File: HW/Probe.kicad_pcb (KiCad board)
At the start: 2 copper layers, 250 x 33 mm, 33 parts

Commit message: Update footprints for cam and distance sensor
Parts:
- CAM: footprint Connector_PinHeader_1.27mm:PinHeader_1x08_P1.27mm_Vertical -> Connector_PinHeader_2.54mm:PinHeader_1x08_P2.54mm_Vertical
- DIST: footprint Connector_PinHeader_1.27mm:PinHeader_1x05_P1.27mm_Vertical -> Connector_PinSocket_2.54mm:PinSocket_1x05_P2.54mm_Vertical
- moved CAM 4.44 mm to (231.3, 85.6)
- moved DIST 3.20 mm to (266.6, 99.5)
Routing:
- net SCL: track 242.5 -> 234.7 mm, vias 0 -> 2
- net DIST_INT: track 223.2 -> 227.8 mm
- net 3V3: track 225.2 -> 228.3 mm
- net CS: track 193.7 -> 196.3 mm
- net MOSI: track 182.7 -> 180.4 mm
- net MISO: track 187.4 -> 185.6 mm
- net +5V: track 264.8 -> 263.5 mm
- net SDA: track 237.1 -> 236.3 mm
- added copper zone on F.Cu, net GND

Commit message: Update PCB
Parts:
- removed NUCLEO-L432KC: NUCLEO-L432KC, Downloads:MODULE_NUCLEO-L432KC
- removed R: R, Resistor_SMD:R_0603_1608Metric
- removed USB: USB_C_Receptacle_USB2.0, KiCad:2171820001
- added Nucleo-L432KC1: ~, Library:MODULE_NUCLEO-L432KC, F.Cu at (67.5, 94.2)
- added R1: 100, Resistor_SMD:R_0603_1608Metric, F.Cu at (57.2, 81.1)
- added R2: 5.1K, Resistor_SMD:R_0603_1608Metric, F.Cu at (34.7, 93.0)
- added R3: 5.1K, Resistor_SMD:R_0603_1608Metric, F.Cu at (34.7, 96.1)
- added USB1: USB4110-GF-A_REVB, Library:GCT_USB4110-GF-A_REVB, F.Cu at (28.7, 94.5)
- CAM1: renamed from CAM; footprint Connector_PinHeader_2.54mm:PinHeader_1x08_P2.54mm_Vertical -> Connector_PinSocket_2.54mm:PinSocket_1x08_P2.54mm_Vertical
- H1, H10, H11, H12, H13, H14, H17, H18, H19, H2, H20, H3, H4, H5, H6, H7, H8, H9: footprint MountingHole:MountingHole_3.2mm_M3_Pad -> MountingHole:MountingHole_3.2mm_M3_Pad_Via
- moved LSR_PWR1 3.48 mm to (96.5, 92.8), turned to 180 degrees
- moved DIST1 1.30 mm to (265.3, 99.5)
- moved LED_SIG1 0.73 mm to (96.5, 104.2)
- moved LSR_SIG1 0.73 mm to (96.5, 82.2)
- moved LED_PWR1 0.64 mm to (96.5, 96.5)
- renumbered DIST to DIST1, LED+ to LED+1, LED- to LED-1, LED_OUT to LED_OUT1, LED_PWR to LED_PWR1, LED_SIG to LED_SIG1, LSR+ to LSR+1, LSR- to LSR-1, LSR_OUT to LSR_OUT1, LSR_PWR to LSR_PWR1, LSR_SIG to LSR_SIG1
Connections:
- net SCL renamed /SCL
- net SDA renamed /SDA
- CAM1 pad 1: CS -> /CS
- CAM1 pad 2: MOSI -> /MOSI
- CAM1 pad 3: MISO -> /MISO
- CAM1 pad 4: SCK -> /SCK
- DIST1 pad 1: 3V3 -> +3.3V
- DIST1 pad 4: DIST_INT -> /INT
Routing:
- net +3.3V: track 0.00 -> 236.9 mm, vias 0 -> 1
- net 3V3: track 228.3 -> 0.00 mm, vias 1 -> 0
- net DIST_INT: track 227.8 -> 0.00 mm, vias 2 -> 0
- net /INT: track 0.00 -> 227.2 mm, vias 0 -> 1
- net /CS: track 0.00 -> 217.3 mm
- net CS: track 196.3 -> 0.00 mm
- net /MOSI: track 0.00 -> 187.1 mm, vias 0 -> 2
- net /MISO: track 0.00 -> 186.1 mm
- net SCK: track 186.1 -> 0.00 mm
- net MISO: track 185.6 -> 0.00 mm
- net /SCK: track 0.00 -> 185.4 mm
- net MOSI: track 180.4 -> 0.00 mm
- net /D-: track 0.00 -> 61.7 mm
- net D-: track 59.0 -> 0.00 mm
- net /D+: track 0.00 -> 58.3 mm
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- removed copper zone on F.Cu, net +5V
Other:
- outline, holes or cut-outs redrawn
- board text added: "CAMERA"
- board text added: "DISTANCE"
- board text added: "LED+"
- board text added: "LED-"
- board text added: "LED_OUT"
- board text added: "LED_PWR"
- board text added: "LED_SIG"
- board text added: "LSR+"
- board text added: "LSR-"
- board text added: "LSR_OUT"
- board text added: "LSR_PWR"
- board text added: "LSR_SIG"
- board text added: "NUCLEO L432KC"
- board text added: "USB4110 GF-A"

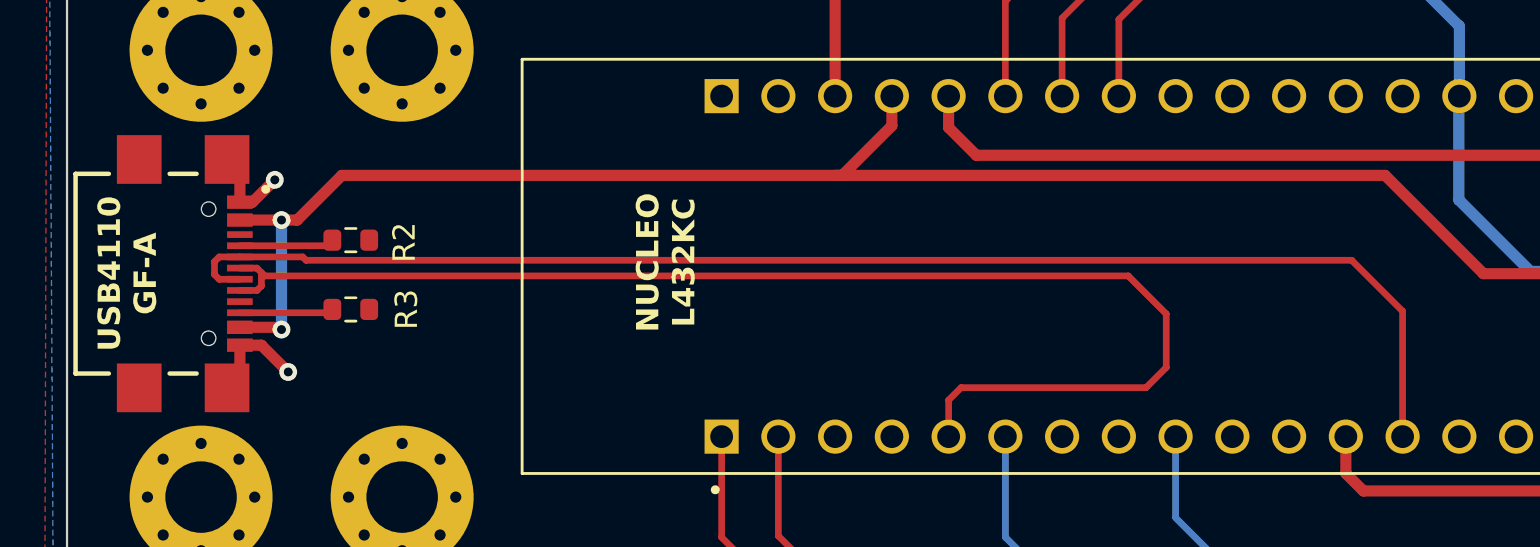
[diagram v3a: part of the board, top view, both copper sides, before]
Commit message: Change USB footprint, label PCB
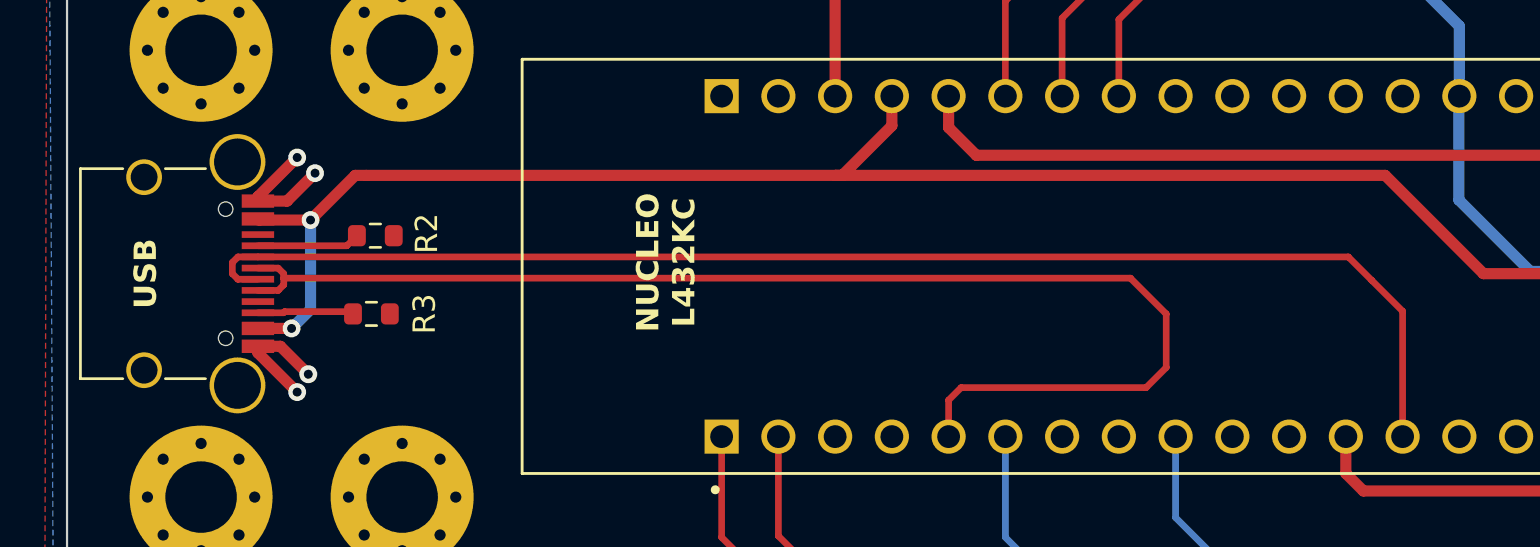
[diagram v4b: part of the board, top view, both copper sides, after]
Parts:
- USB1: value USB4110-GF-A_REVB -> USB_C_Receptacle_USB2.0; footprint Library:GCT_USB4110-GF-A_REVB -> Library:USB_C_Receptacle_HRO_TYPE-C-31-M-12_Circle_Hole
- moved USB1 2.16 mm to (26.5, 94.5)
- moved R2 1.12 mm to (35.8, 92.8)
- moved R3 0.95 mm to (35.6, 96.3)
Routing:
- net GND: track 26.8 -> 29.2 mm, vias 3 -> 5
- net +5V: track 232.8 -> 231.9 mm
- net /D-: track 61.7 -> 60.9 mm
- net /D+: track 58.3 -> 57.6 mm
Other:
- board text added: "Procházka & Malaník Nucleo Based Profilometer v.1 2023"
- board text added: "USB"
- board text removed: "USB4110 GF-A"
